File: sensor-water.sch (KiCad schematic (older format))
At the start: 82 parts, among them IC1 STM8S003F3P-RESCUE-sensor-wat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, P1 CONN_01X04, P2 CONN_01X01, P3 CONN_01X04, P4 CONN_01X03, P5 CONN_01X01, P6 CONN_01X01, P7 CONN_01X01, P8 CONN_01X01, P9 CONN_01X01, Q1 C1815, Q2 C1815, U1 LM358D, U10 -6V5, U11 -6V5, U12 LP2985LV, U16 LM324, U3 -6V5, U4 TC7660, U5 -6V5, U6 -6V5, U7 -6V5, U8 -6V5, U9 LM358

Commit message: initial README.md
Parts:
- removed U10, U11, U3, U5, U6, U7, U8: -6V5, mylib:VCC, symbol -6V5
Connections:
- net -9VA: now reaches U1.4 (-)
- net -9VA: now also C11.1, C13.1, C14.1, C15.1, C16.1, C3.1, U1.4 (-), U16.11 (-), U16.4 (+), U16.4 (+), U16.4 (+), U4.5 (Vout), U9.4 (-), U9.4 (-)
- net +9VA: now reaches U1.8 (+)
- net +9VA: now also C2.2, C4.2, C5.2, C6.2, C8.2, C9.2, P1.4 (P4), U1.8 (+), U12.1 (VIN), U12.3 (ON/OFF), U16.11 (-), U16.11 (-), U16.11 (-), U16.4 (+), U4.8 (V+), U9.8 (+), U9.8 (+)

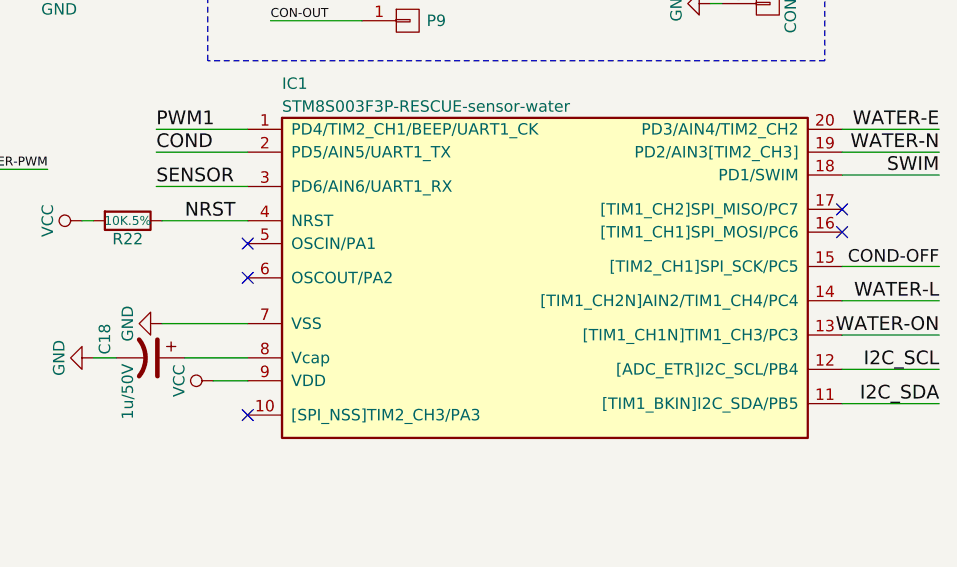
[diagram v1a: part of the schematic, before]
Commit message: initial kicad-sensor-water
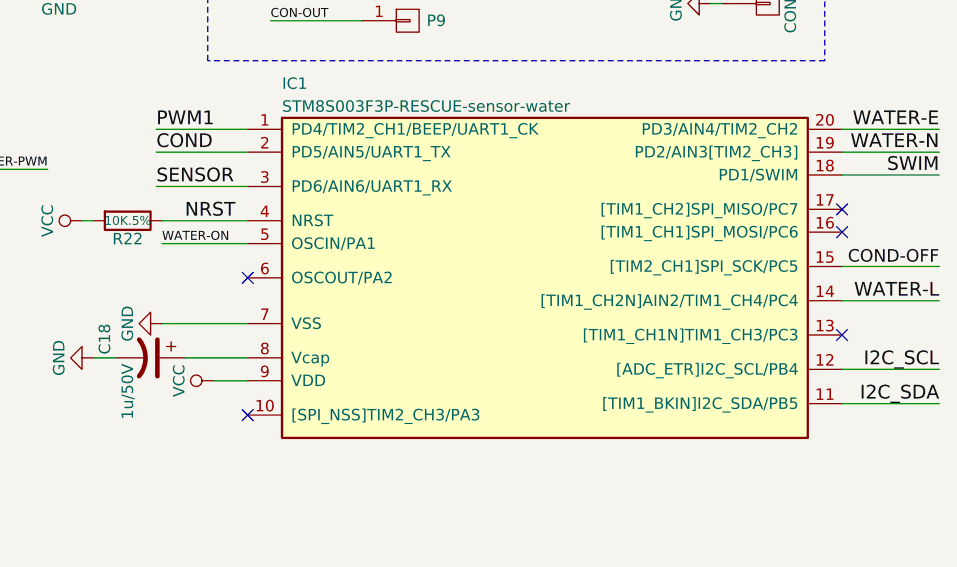
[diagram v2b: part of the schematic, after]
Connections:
- net WATER-ON: now also IC1.5 (OSCIN/PA1); no longer IC1.13 ([TIM1_CH1N]TIM1_CH3/PC3)

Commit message: initial kicad-sensor-water
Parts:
- removed C1, C3: 100nF/10V, mylib:C_2920, symbol CAP
- removed C11, C13: 100nF/50V, mylib:C_2920, symbol CAP
- removed C18: 1u/50V, Capacitors_SMD:C_0805, symbol CP1
- removed IC1: STM8S003F3P-RESCUE-sensor-water, Housings_SOIC:SOIC-20_7.5x12.8mm_Pitch1.27mm, symbol STM8S003F3P-RESCUE-sensor-water
- removed P4: CONN_01X03, Pin_Headers:Pin_Header_Angled_1x03, symbol CONN_01X03
- added C1, C3: 100uF/16V, Capacitors_SMD:C_1206_HandSoldering, symbol CP1
- added IC1: STM32F030F4P6, mylib:STM32F030F4P6, symbol STM32F030F4P6
- added R26: 10K, Resistors_SMD:R_0805_HandSoldering, symbol R
- added U2: DS18B20, TO_SOT_Packages_THT:TO-92_Horizontal2_Inline_Narrow_Oval, symbol DS18B20
- C10, C12, C14, C15, C16, C6, C7, C8, C9: footprint mylib:C_2920 -> Capacitors_SMD:C_0805_HandSoldering
- C2: value 10nF/10V -> 10uF/16V; footprint Capacitors_SMD:C_0805_HandSoldering -> Capacitors_SMD:C_1206_HandSoldering
- C4, C5: value 100nF/50V -> 100nF/16V; footprint mylib:C_2920 -> Capacitors_SMD:C_0805_HandSoldering
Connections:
- net COND: now also IC1.10 (PA4/IN4)
- net COND-OFF: now also IC1.17 (PA9/USART_1/TIM_1/TIM_15/I2C_SCL)
- net GND: now also C5.2, P3.4 (P4), C3.1, IC1.15 (VSS), R26.2, U2.1 (GND); no longer C5.1, P3.3 (P3)
- net I2C_SCL: now also IC1.3 (PF1-OSC_OUT/I2C_SCL)
- net I2C_SDA: now also IC1.2 (EPF0-OSC_IN/I2C_SDA)
- net NRST: now also IC1.4 (NRST); no longer P3.4 (P4)
- net PWM1: now also IC1.12 (PA6/PWN_CH)
- net SENSOR: now also IC1.9 (PA3/IN3), U2.2 (DQ)
- net WATER-E: now also IC1.8 (PA2/IN2)
- net WATER-L: now also IC1.6 (PA0/IN0)
- net WATER-N: now also IC1.7 (PA1/IN1)
- net WATER-ON: now also IC1.18 (PA10/USART_RX/TIM1/TIM15/I2C_SCL)
- net at U4.2 (CAP+): now also C1.1
- net at U4.4 (CAP-): now also C1.2
- net +9VA renamed +12V
- net +12V: no longer C4.2, C5.2
- net -9VA renamed -12VA
- net -12VA: now also C3.2
- net SWIM renamed SWDIO
- net SWDIO: now also IC1.19 (PA13/IR_OUT/SWDIO)
- net VCC renamed +3V3
- net +3V3: now also C4.2, C5.1, IC1.16 (VDD), IC1.5 (VDDA), U2.3 (VDD)
- new net: IC1.1 (BOOT0), R26.1
- new net SWCLK: IC1.20 (PA14/USART1_TX/USART2_TX/SMCLK), P3.3 (P3)
- no-connect marks 8 -> 6
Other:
- moved on the sheet: C14, C15, C16, C19, C20, C6, C8, C9, R22, U12
